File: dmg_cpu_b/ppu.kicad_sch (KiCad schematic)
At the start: 0 parts

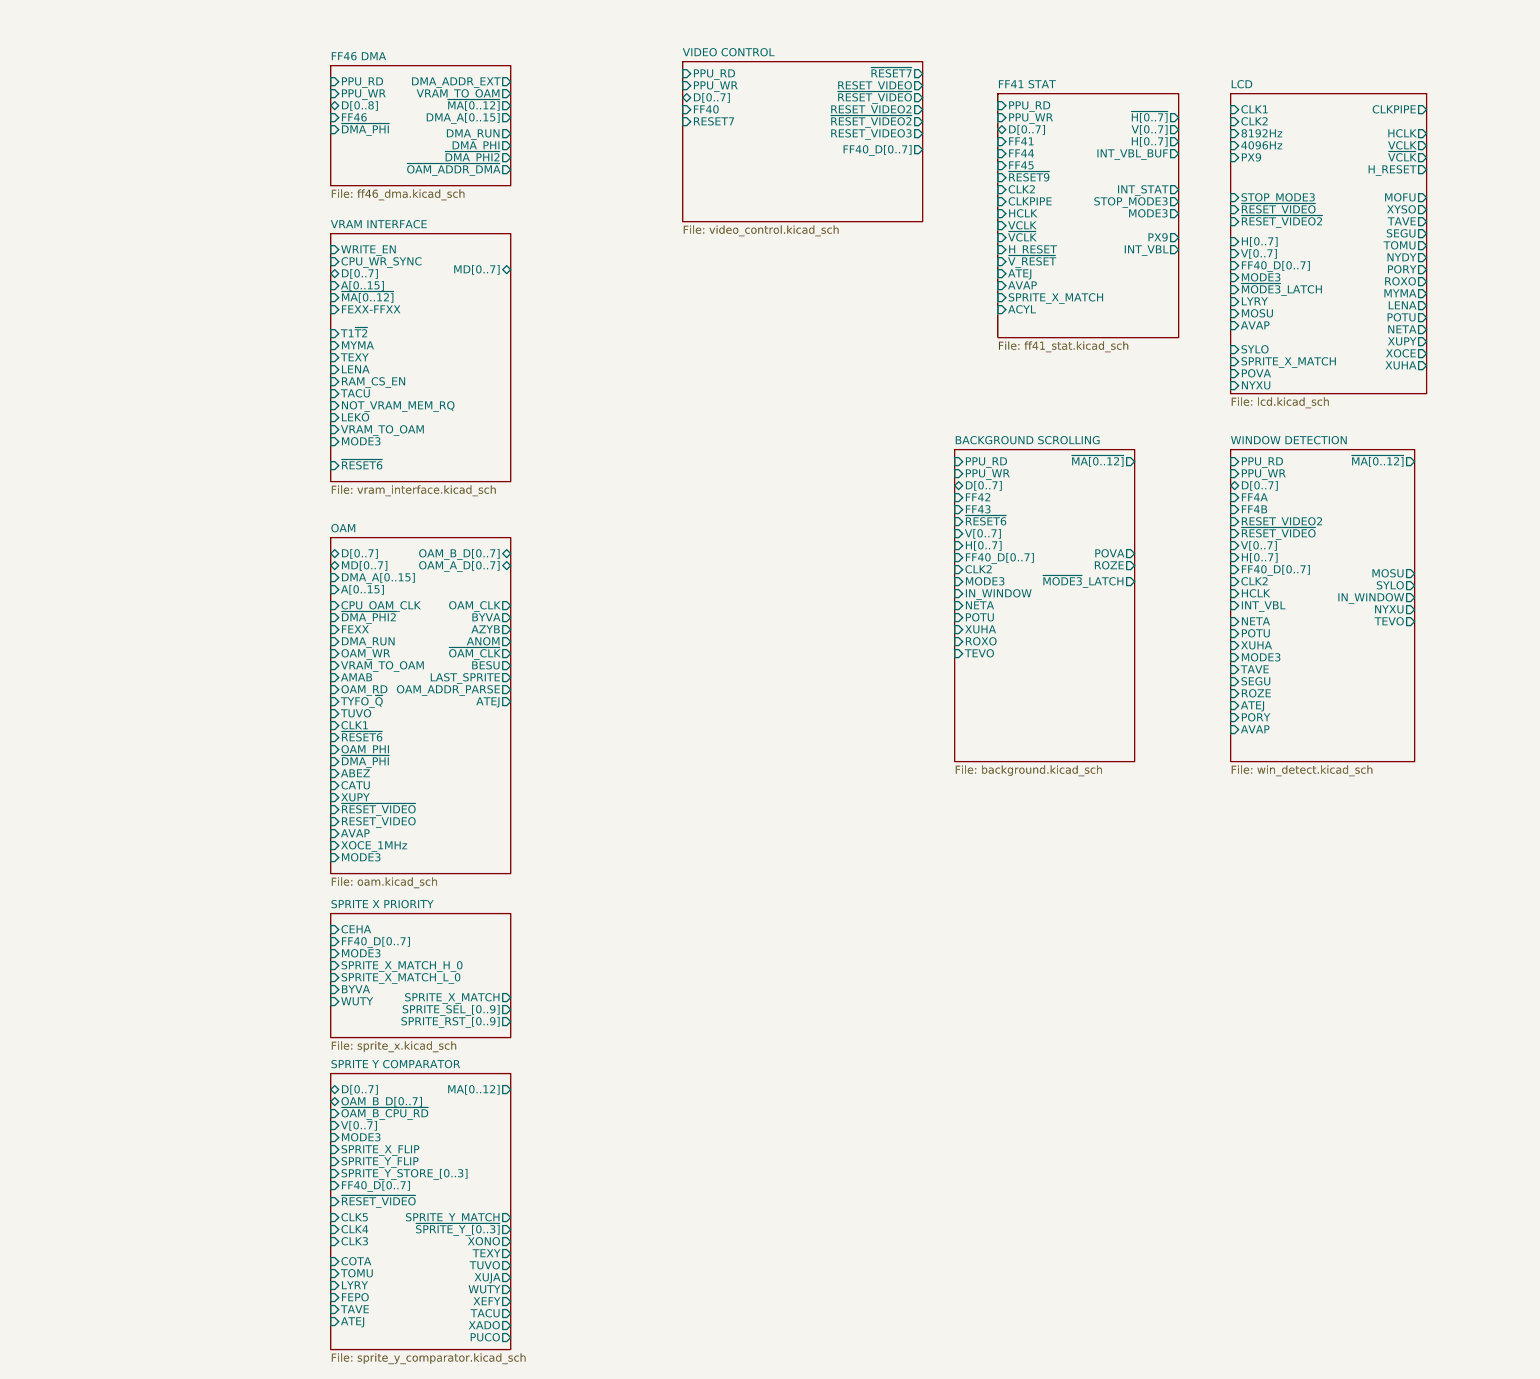
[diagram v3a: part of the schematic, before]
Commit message: more oam sheets added. Some are still work in progress.
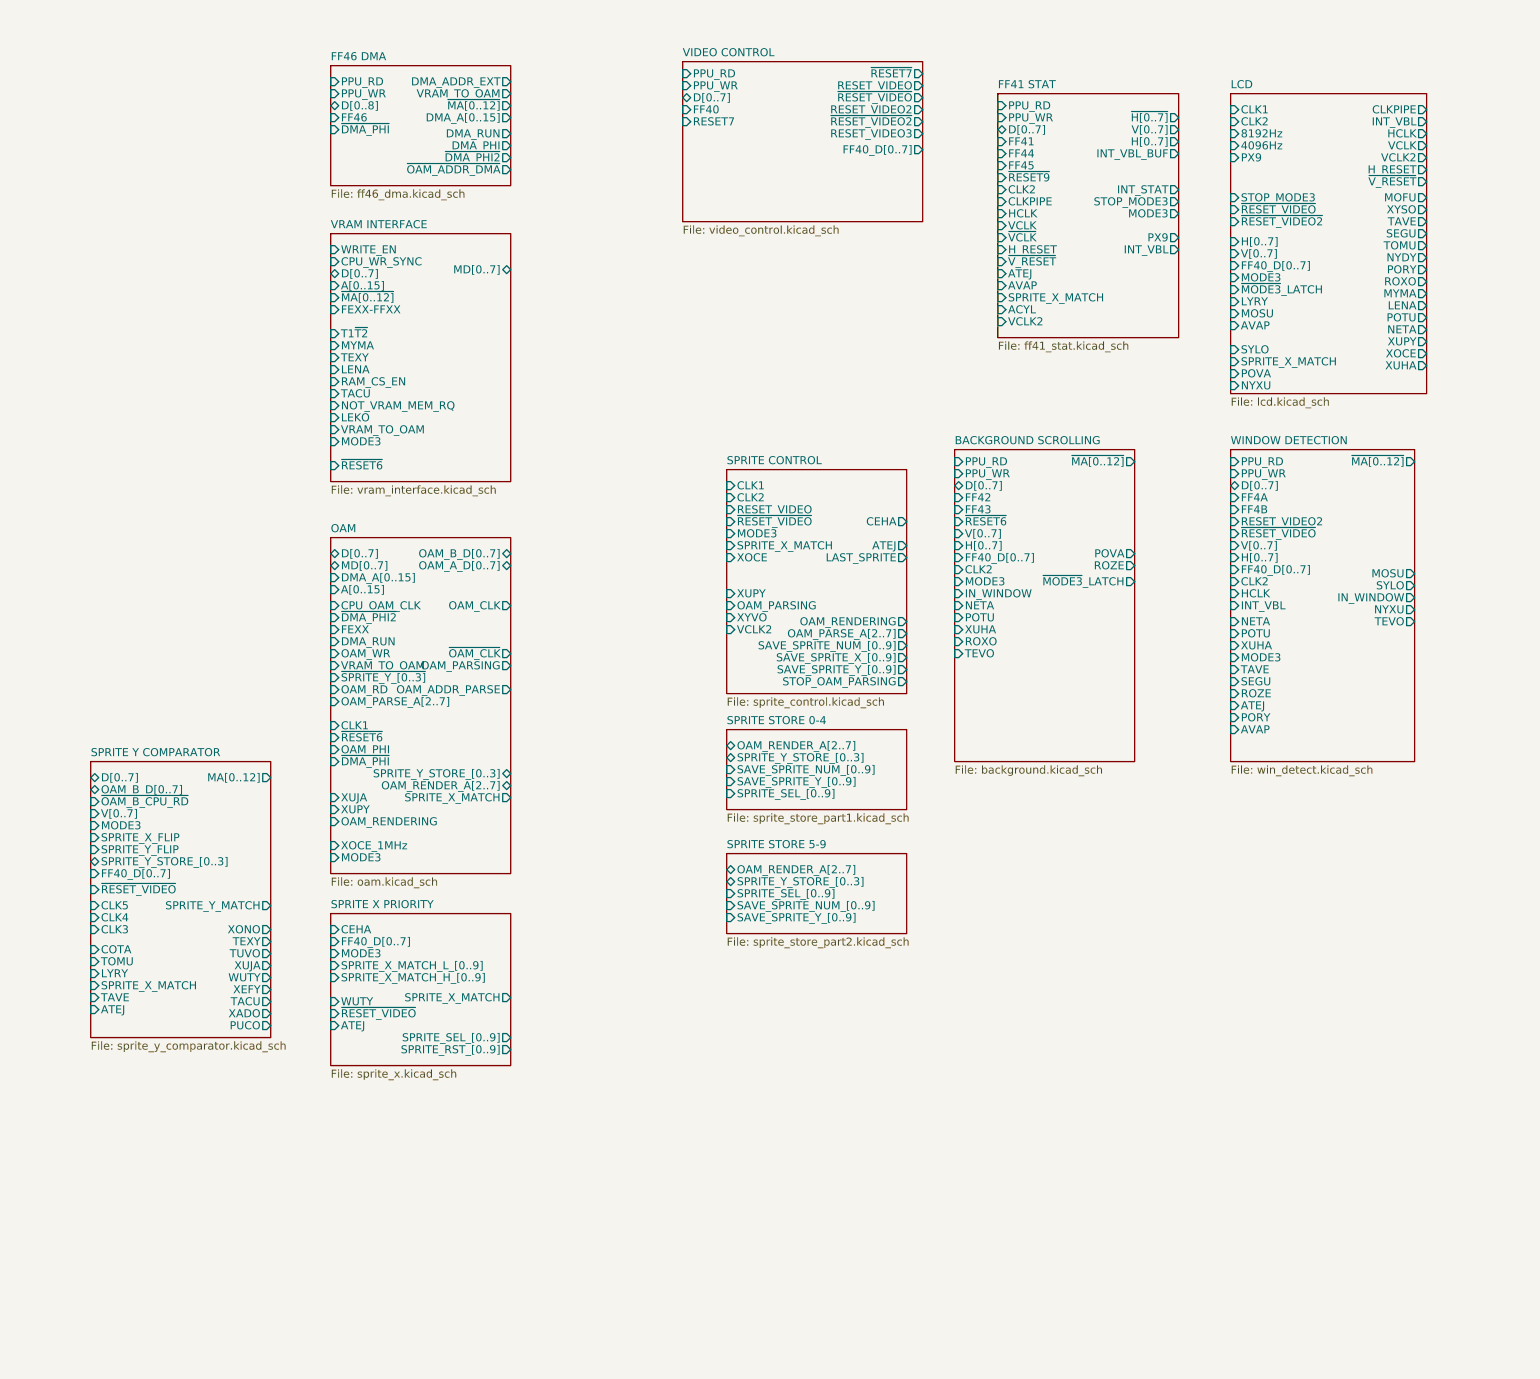
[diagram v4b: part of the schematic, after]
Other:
- added sheet SPRITE CONTROL (sprite_control.kicad_sch)
- added sheet SPRITE STORE 0-4 (sprite_store_part1.kicad_sch)
- added sheet SPRITE STORE 5-9 (sprite_store_part2.kicad_sch)
- sheet FF41 STAT ports: added VCLK2; removed none
- sheet LCD ports: added INT_VBL, VCLK2, ~{V_RESET}; removed ~{VCLK}
- sheet OAM ports: added OAM_PARSE_A[2..7], OAM_PARSING, OAM_RENDERING, OAM_RENDER_A[2..7], SPRITE_X_MATCH, SPRITE_Y_STORE_[0..3], XUJA, ~{SPRITE_Y_[0..3]}; removed ABEZ, AMAB, ANOM, ATEJ, AVAP, AZYB, BESU, BYVA, CATU, LAST_SPRITE, RESET_VIDEO, TUVO, TYFO_~{Q}, ~{RESET_VIDEO}
- sheet SPRITE X PRIORITY ports: added ATEJ, SPRITE_X_MATCH_H_[0..9], SPRITE_X_MATCH_L_[0..9], ~{RESET_VIDEO}; removed BYVA, SPRITE_X_MATCH_H_0, SPRITE_X_MATCH_L_0
- sheet SPRITE Y COMPARATOR ports: added SPRITE_X_MATCH; removed FEPO, ~{SPRITE_Y_[0..3]}

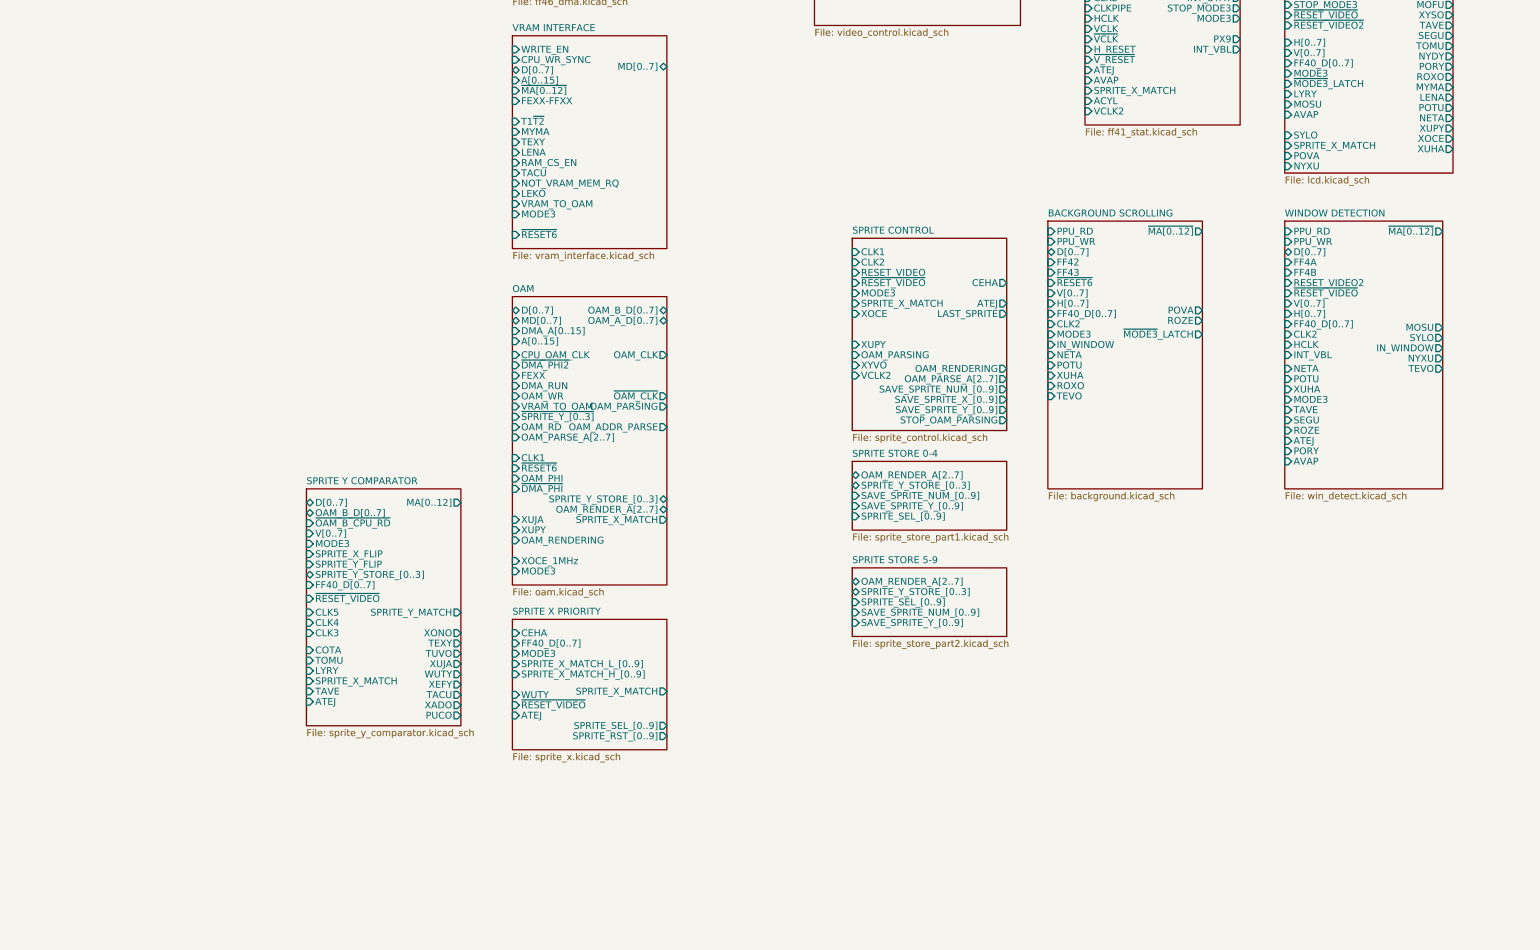
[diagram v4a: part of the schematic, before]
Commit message: More OAM sheets added.
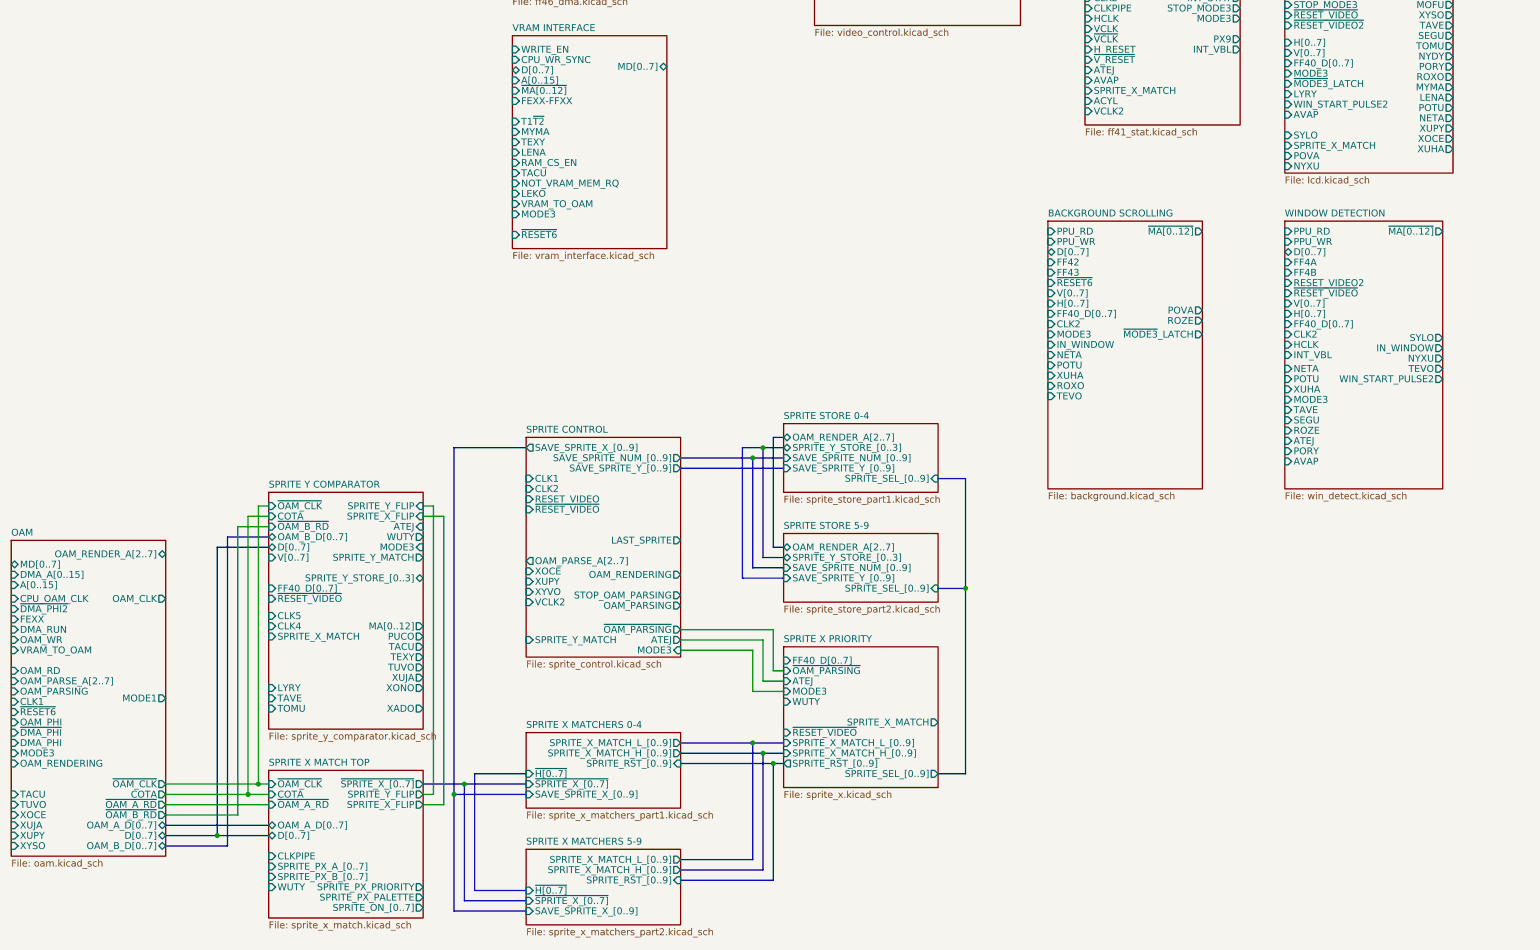
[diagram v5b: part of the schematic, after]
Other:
- added sheet SPRITE X MATCH TOP (sprite_x_match.kicad_sch)
- added sheet SPRITE X MATCHERS 0-4 (sprite_x_matchers_part1.kicad_sch)
- added sheet SPRITE X MATCHERS 5-9 (sprite_x_matchers_part2.kicad_sch)
- sheet LCD ports: added WIN_START_PULSE2; removed MOSU
- sheet OAM ports: added COTA, DMA_PHI, MODE1, TACU, TUVO, XOCE, XYSO, ~{OAM_A_RD}, ~{OAM_B_RD}; removed OAM_ADDR_PARSE, SPRITE_X_MATCH, SPRITE_Y_STORE_[0..3], XOCE_1MHz, ~{SPRITE_Y_[0..3]}
- sheet SPRITE CONTROL ports: added SPRITE_Y_MATCH, ~{OAM_PARSING}; removed CEHA, SPRITE_X_MATCH
- sheet SPRITE X PRIORITY ports: added ~{OAM_PARSING}; removed CEHA
- sheet SPRITE Y COMPARATOR ports: added ~{OAM_B_RD}, ~{OAM_CLK}; removed CLK3, XEFY, ~{OAM_B_CPU_RD}
- sheet WINDOW DETECTION ports: added WIN_START_PULSE2; removed MOSU

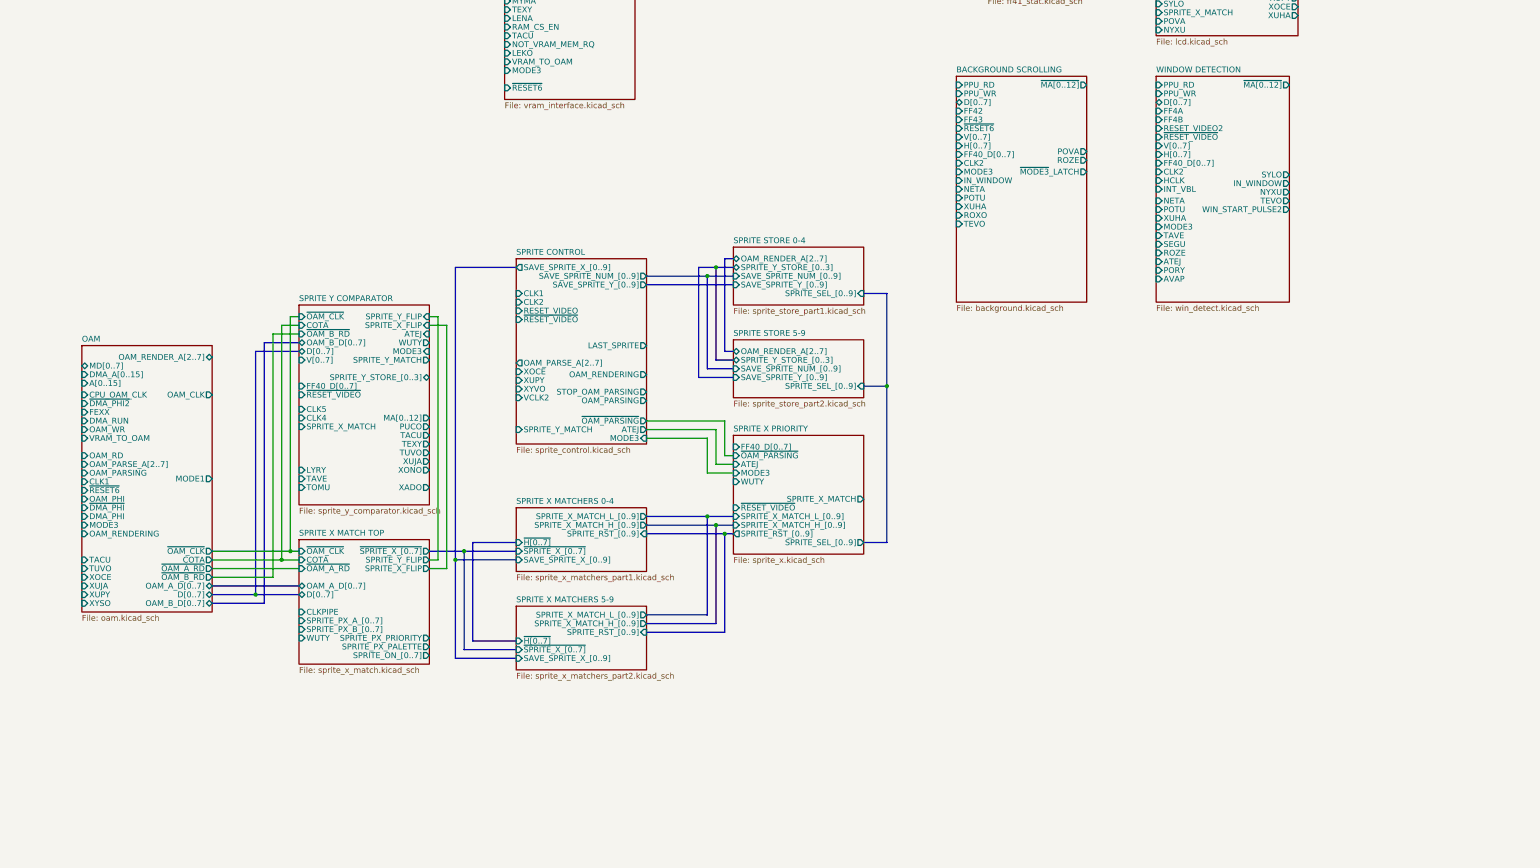
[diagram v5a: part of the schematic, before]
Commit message: bg and sp px shifters added.
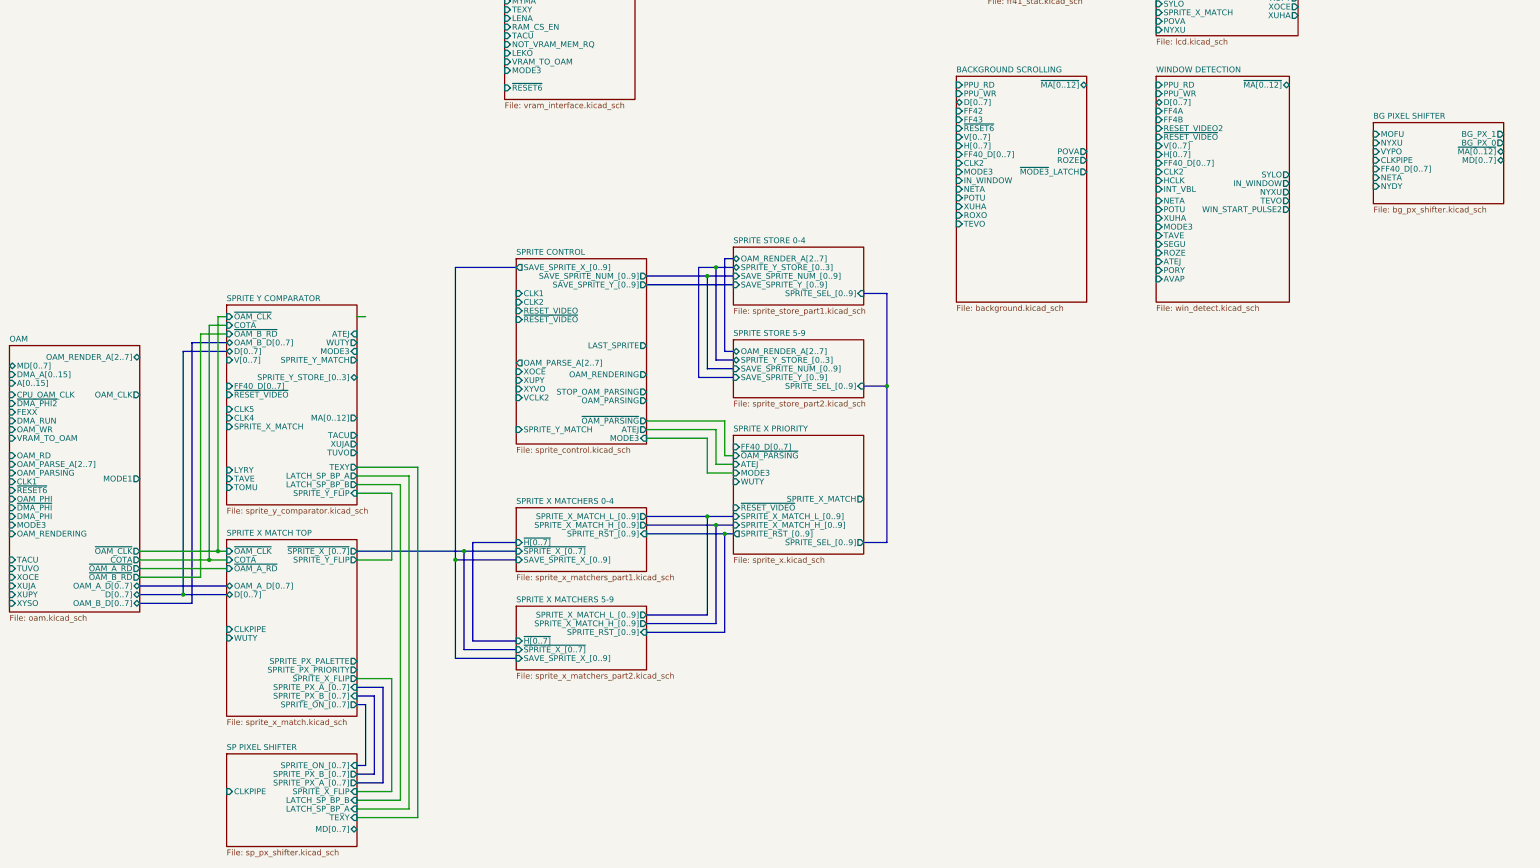
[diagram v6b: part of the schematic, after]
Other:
- added sheet BG PIXEL SHIFTER (bg_px_shifter.kicad_sch)
- added sheet SP PIXEL SHIFTER (sp_px_shifter.kicad_sch)
- sheet SPRITE Y COMPARATOR ports: added LATCH_SP_BP_A, LATCH_SP_BP_B; removed PUCO, SPRITE_X_FLIP, XADO, XONO
